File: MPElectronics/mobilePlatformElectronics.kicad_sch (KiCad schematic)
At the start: 40 parts, among them J1 UART, J2 CommandGenerator, M1 Motor_DC, M2 Motor_DC, Q1 LTR3208E, SW2 Reset, U1 PIC32MX170F256B, U2 L293NE/SN754410NE, U7 MCP6294, U8 LM339AN

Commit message: progress on schematic; complete pin assignment; most subsystems designed electrically
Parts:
- removed J2: CommandGenerator, symbol Connector:Conn_01x04_Socket
- removed M1, M2: Motor_DC, symbol Motor:Motor_DC_ALT
- added C10: 10uF, symbol ME218_BaseLib:Cap
- added C11, C12, C14, C15, C16, C7, C8, C9: 0.1uF, symbol ME218_BaseLib:Cap
- added J2: UART, symbol Connector:Conn_01x02_Socket
- added J3, J4: Magnetic Encoder, symbol Connector:Conn_01x04_Socket
- added M1 (x2), M2 (x2): Motor_DC, symbol Motor:Motor_DC_ALT
- added M3: SG90 9g Micro Servo, symbol ME218_BaseLib:Motor_Servo
- added M4, M5: Servo, symbol ME218_BaseLib:Motor_Servo
- added PRG2: MPLAB_Snap, symbol ME218_BaseLib:MPLAB_Snap
- added R12, R14: 1K, symbol ME218_BaseLib:Res2
- added R13, R15: 10K, symbol ME218_BaseLib:Res2
- added SW1, SW3: Reset, symbol ME218_BaseLib:SW-PB
- added SW4, SW5: SW_SPDT, symbol Switch:SW_SPDT
- added U10, U2: TLE5206-2S, TLE5206-2S:TO127P1000X440X1730-7, symbol TLE5206-2S:TLE5206-2S
- added U11, U12, U13: IR Distance, OptoDevice:Vishay_MINICAST-3Pin, symbol Sensor_Proximity:TSSP58038
- added U3: PIC32MX170F256B, symbol ME218_BaseLib:PIC32MX170F256B
- added U4, U5, U6, U9: IR Line Sensor, OptoDevice:Vishay_MINICAST-3Pin, symbol Sensor_Proximity:TSSP58038
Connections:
- net +3V3: now also C7.1, C8.2, J3.1 (Pin_1), J4.1 (Pin_1), PRG2.2 (Vdd), R13.2, R15.2, SW4.1 (A), SW5.1 (A), U11.3 (Vs), U12.3 (Vs), U13.3 (Vs), U3.13 (Vdd), U3.28 (AVdd), U4.3 (Vs), U5.3 (Vs), U6.3 (Vs), U9.3 (Vs)
- net +5V: now also U2.1 (EN1,2), U2.9 (EN3,4), C16.2, M3.2 (+), M4.2 (+), M5.2 (+); no longer C5.2
- net GND: now also C1.2, C2.1, C3.1, C4.2, C5.1, PRG1.3 (Vss), SW2.2, U1.19 (Vss), U1.27 (AVss), U1.8 (Vss), U2.10 (3A), U2.12 (GND), U2.13 (GND), U2.4 (GND), U2.5 (GND), U2.7 (2A), C10.1, C11.2, C12.1, C14.1, C15.1, C16.1, C7.2, C8.1, C9.2, J3.4 (Pin_4), J4.4 (Pin_4), M3.3 (-), M4.3 (-), M5.3 (-), PRG2.3 (Vss), SW1.2, SW3.2, SW4.3 (C), SW5.3 (C), U10.4 (GND), U11.2 (GND), U12.2 (GND), U13.2 (GND), U2.4 (GND), U3.19 (Vss), U3.27 (AVss), U3.8 (Vss), U4.2 (GND), U5.2 (GND), U6.2 (GND), U9.2 (GND)
- net GNDREF: no longer C1.2, C2.1, C3.1, C4.2, C5.1, PRG1.3 (Vss), SW2.2, U1.19 (Vss), U1.27 (AVss), U1.8 (Vss), U2.12 (GND), U2.13 (GND), U2.4 (GND), U2.5 (GND)
- net RX: now also J2.1 (Pin_1), U3.16 (5VT/RB7)
- net SPI1_SCK: now also U3.25 (RB14)
- net SPI1_SDI: now also U3.22 (RB11)
- net SPI1_SDO: now also U3.24 (RB13)
- net TX: now also J2.2 (Pin_2), U3.15 (PGEC3/5VT/RB6)
- net at D1.2 (A), D2.1 (K), D3.1 (KA)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: now also M1.1 (+)
- net at D10.2 (A), D11.1 (K), D12.1 (KA)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: now also M2.1 (+)
- net INT_LINE_FRONT_R: now reaches U1.9 (RA2)
- net INT_LINE_FRONT_R: now also U6.1 (OUT); no longer U2.1 (EN1,2)
- net at D13.2 (A), D14.1 (K), R23.1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: now also M2.2 (-)
- net at D4.2 (A), D5.1 (K), R3.1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: now also M1.2 (-)
- net DIN_LINE_PIVOT_L: now reaches U1.6 (RB2)
- net DIN_LINE_PIVOT_L: now also U4.1 (OUT); no longer U2.9 (EN3,4)
- net IC_DISTANCE: now reaches U1.14 (PGED3/5VT/RB5)
- net IC_DISTANCE: now also U11.1 (OUT)
- net M_DRIVE_L_PWM: now reaches U1.17 (5VT/RB8)
- net M_DRIVE_L_PWM: now also U2.3 (IN1)
- net M_DRIVE_R_PWM: now reaches U1.21 (PGEC2/5VT/RB10)
- net M_DRIVE_R_PWM: now also U10.3 (IN1)
- net M_DRIVE_R_DIR: now reaches U1.23 (RB12)
- net M_DRIVE_R_DIR: now also U10.5 (IN2)
- net DIN_LINE_PIVOT_R: now reaches U1.7 (RB3)
- net DIN_LINE_PIVOT_R: now also U9.1 (OUT)
- net IC renamed IC_BEACON
- net IC_BEACON: now also U1.12 (RA4); no longer U1.18 (PGED2/5VT/RB9)
- net LINE_OUT renamed INT_DRIVE_L
- net INT_DRIVE_L: now also J3.2 (Pin_2)
- net RA1, pin 3, OC2, Direction Pin renamed INT_DRIVE_R
- net INT_DRIVE_R: now also J4.2 (Pin_2); no longer U2.7 (2A)
- net RA3, pin 10, OC3 renamed INT_LINE_FRONT_L
- net INT_LINE_FRONT_L: now also U5.1 (OUT); no longer U2.10 (3A)
- net RA4, pin 12, OC4 or OC5, Direction Pin renamed M_INTAKE_PWM
- net M_INTAKE_PWM: now also U2.2 (1A), U3.6 (RB2); no longer U1.12 (RA4)
- net RB15, pin 26, OC1 renamed SPI1_~{CS}
- net SPI1_~{CS}: now also U3.26 (RB15); no longer U2.2 (1A)
- new net: PRG2.1 (~{MCLR}/Vpp), R14.1, U3.1 (~{MCLR})
- new net: PRG2.4 (PGData), U3.4 (PGED1/RB0)
- new net: PRG2.5 (PGClk), U3.5 (PGEC1/RB1)
- new net: C9.1, R12.2, R13.1, SW1.1
- new net: M1.1 (+), U2.1 (OUT1)
- new net: M1.2 (-), U2.7 (OUT2)
- new net: C11.1, R14.2, R15.1, SW3.1
- new net: C10.2, U3.20 (Vcap)
- new net: M2.1 (+), U10.1 (OUT1)
- new net: M2.2 (-), U10.7 (OUT2)
- new net +14V: C12.2, C14.2, C15.2, C5.2, U10.6 (VS), U2.6 (VS)
- new net DIN_CARGO_IN: U12.1 (OUT), U3.17 (5VT/RB8)
- new net DIN_CARGO_OUT: U13.1 (OUT), U3.18 (PGED2/5VT/RB9)
- new net DIN_GAMEMODE: SW4.2 (B), U3.11 (RB4)
- new net DIN_START: R12.1, U3.10 (RA3)
- new net DIN_STRATEGY: SW5.2 (B), U3.12 (RA4)
- new net M_ARM_ELBOW_PWM: M4.1 (PWM), U3.2 (RA0)
- new net M_ARM_HAND_PWM: M5.1 (PWM), U3.3 (RA1)
- new net M_BG_PWM: M3.1 (PWM), U3.21 (PGEC2/5VT/RB10)
- new net M_DRIVE_L_DIR: U1.18 (PGED2/5VT/RB9), U2.5 (IN2)
- new net M_FEEDER_PWM: U3.9 (RA2)
- new net bL: J3.3 (Pin_3)
- new net bR: J4.3 (Pin_3)
- no-connect marks 5 -> 7
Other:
- note removed: "Pololu QTR Reflectance Sensor"
- moved on the sheet: C1, C13, C2, C3, C4, C6, D1, D10, D11, D12, D13, D14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

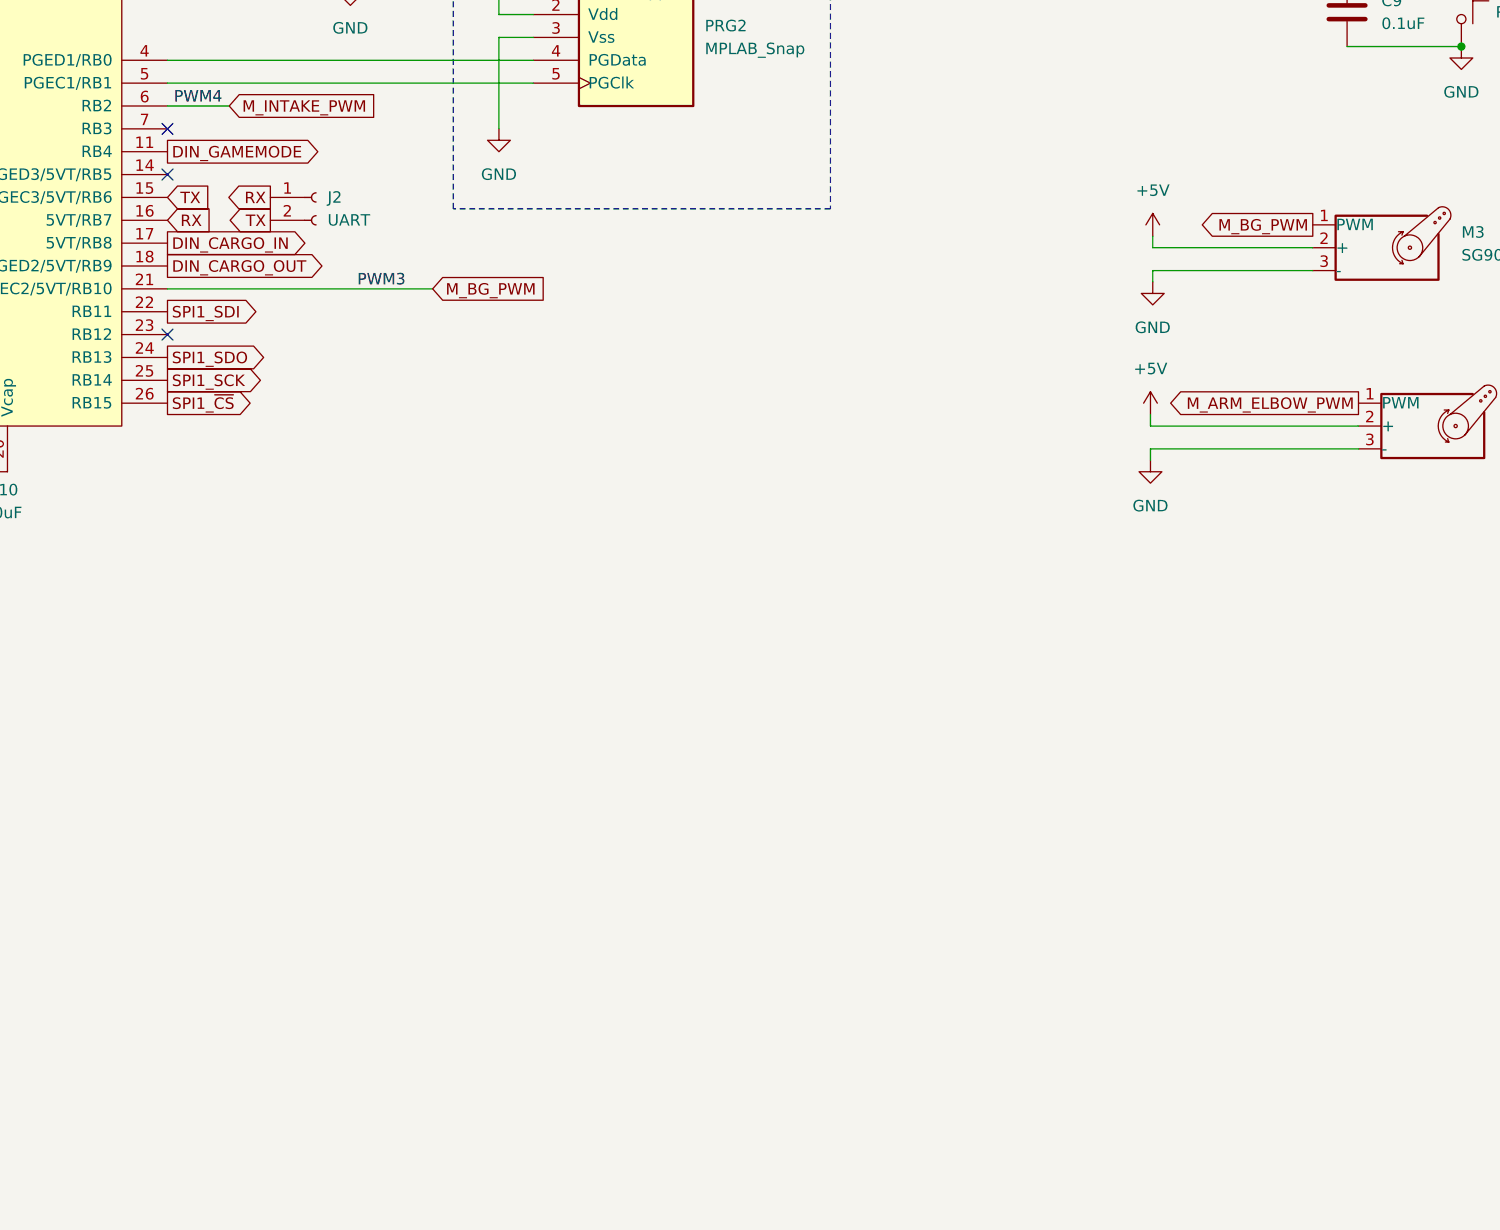
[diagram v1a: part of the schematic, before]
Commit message: update schematic
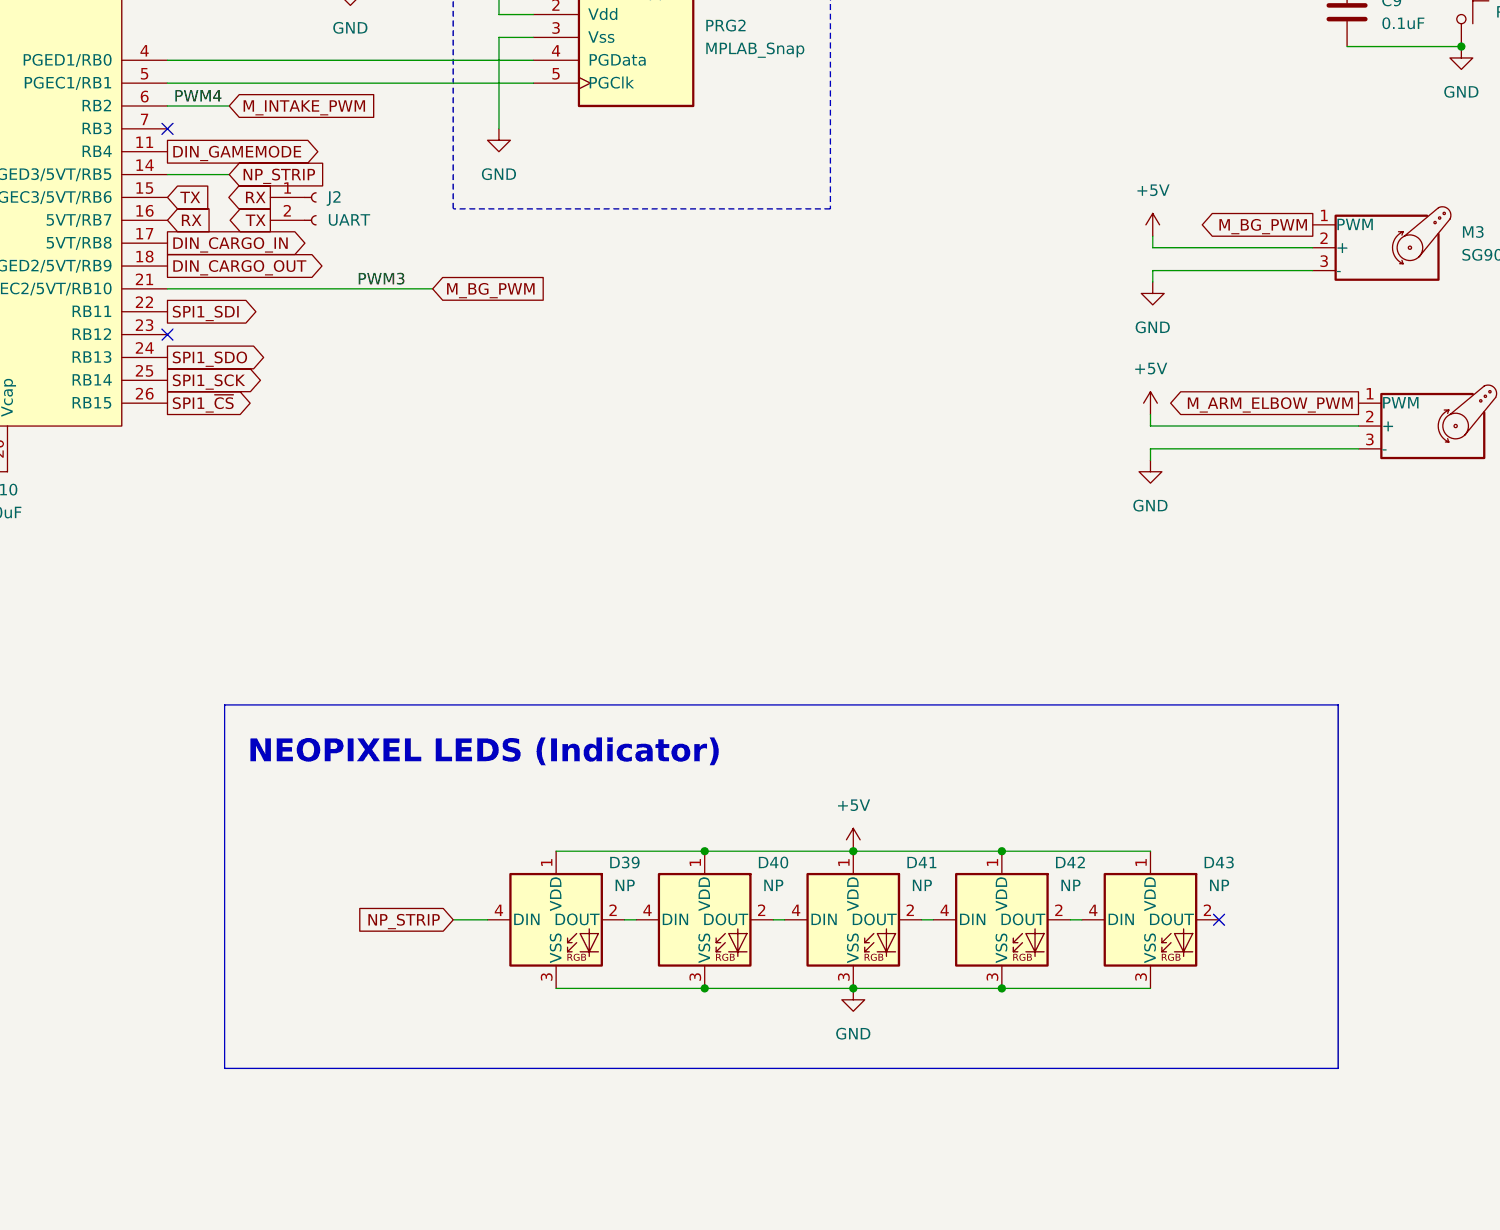
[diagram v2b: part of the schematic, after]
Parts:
- added D39, D40, D41, D42, D43: NP, LED_SMD:LED_WS2812B_PLCC4_5.0x5.0mm_P3.2mm, symbol LED:WS2812B
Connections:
- net +5V: now also D39.1 (VDD), D40.1 (VDD), D41.1 (VDD), D42.1 (VDD), D43.1 (VDD)
- net GND: now also D39.3 (VSS), D40.3 (VSS), D41.3 (VSS), D42.3 (VSS), D43.3 (VSS)
- net NP_STRIP: now reaches U3.14 (PGED3/5VT/RB5)
- net NP_STRIP: now also D39.4 (DIN)
- new net: D39.2 (DOUT), D40.4 (DIN)
- new net: D40.2 (DOUT), D41.4 (DIN)
- new net: D41.2 (DOUT), D42.4 (DIN)
- new net: D42.2 (DOUT), D43.4 (DIN)
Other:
- note added: "NEOPIXEL LEDS (Indicator)"

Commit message: include stepper driver and stepper in schematic
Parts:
- removed D12, D3: LED_Dual_Bidirectional, symbol Device:LED_Dual_Bidirectional
- removed R23, R3: 100, symbol ME218_BaseLib:Res2
- added A?: A4988_StepperDriver, Module:Pololu_Breakout-16_15.2x20.3mm, symbol Driver_Motor:Pololu_Breakout_A4988
- added M?: SY35ST28-0504A_Stepper_Motor_bipolar, symbol Motor:Stepper_Motor_bipolar
- C14, C5: value 0.1uF -> 470uF
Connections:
- net +14V: now also A?.8 (VMOT)
- net +3V3: now also A?.13 (~{RESET}), A?.14 (~{SLEEP}), A?.2 (VDD)
- net GND: now also A?.1 (GND), A?.16 (DIR), A?.7 (GND), A?.9 (~{ENABLE})
- net M_FEEDER_PWM: now also A?.15 (STEP)
- new net: A?.3 (1B), M?.2 (-)
- new net: A?.4 (1A), M?.1
- new net: A?.5 (2A), M?.3
- new net: A?.6 (2B), M?.4
- no-connect marks 7 -> 10
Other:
- moved on the sheet: D13, D14, D4, D5, M1, M2

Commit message: update schematic; 1 extra pin on drive; 2 extra pins on operator
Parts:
- removed U11: IR Distance, OptoDevice:Vishay_MINICAST-3Pin, symbol Sensor_Proximity:TSSP58038
- added C17: 100uF, symbol ME218_BaseLib:Cap
- added C18, C20: 0.1uF, symbol ME218_BaseLib:Cap
- added C19, C21: 4700uF, symbol ME218_BaseLib:Cap
- added R16, R18: 10K, symbol ME218_BaseLib:Res2
- added R17, R3: 1K, symbol ME218_BaseLib:Res2
- added SW6, SW7: SW_SPDT_LIMIT, symbol Switch:SW_SPDT_XKB_DMx-xxxx-1
- M6: renamed from M4; value Servo -> RDS51150
- M7: renamed from M5; value Servo -> RDS51150
- gave numbers to parts that had none: 2
- renumbered M1 to M3, M2 to M4, M3 to M5, U2 to U14
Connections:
- net +14V: now also C17.2
- net +3V3: now also R16.2, R18.2
- net +5V: no longer M6.2 (+), M7.2 (+)
- net GND: now also C17.1, C18.2, C19.2, C20.2, C21.2, SW6.2 (B), SW7.2 (B)
- net IC_DISTANCE renamed DIN_LIMIT
- net DIN_LIMIT: now also R3.1
- net SPI1_~{SS}: no longer names the net of U1.11 (RB4)
- new net: C20.1, R17.2, R18.1, SW7.1 (A)
- new net: C18.1, R16.1, R3.2, SW6.1 (A)
- new net +12V: C19.1, C21.1, M6.2 (+), M7.2 (+)
- new net DIN_ARM_LIMIT: R17.1
- no-connect marks 10 -> 13
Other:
- note added: "Follow PIC32"
- note added: "Lead PIC32"
- note added: "State Indicator Neopixel"
- note removed: "NEOPIXEL LEDS (Indicator)"
- moved on the sheet: A1, C12, C13, C14, C15, C16, C5, C6, D1, D10, D11, D13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

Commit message: reorganize schematic, label for ease of construction, include improved beacon sensing AFE
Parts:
- added C?: 0.1uF, symbol ME218_BaseLib:Cap
- added R?: 1K, symbol ME218_BaseLib:Res2
- added R?: 470K, symbol ME218_BaseLib:Res2
- added R?: 2K, symbol ME218_BaseLib:Res2
- added unit 4 of U7
- R7: value 100K -> 2K
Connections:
- net +12V is gone; now on net +5V: C19.1, C21.1, M6.2 (+), M7.2 (+)
- net GNDREF is gone; now on net GND: D11.2 (A), D14.2 (A), D2.2 (A), D5.2 (A)
- net +3V3: now also U7.4 (V+)
- net +5V: now also U7.4 (V+); no longer Q1.1 (C), U7.4 (V+)
- net DIN_ARM_LIMIT: now also U3.7 (RB3)
- net DIN_LIMIT: now also U1.12 (RA4); no longer U1.14 (PGED3/5VT/RB5)
- net GND: now also Q1.2 (E), U7.11 (V-)
- net IC_BEACON: now also U1.14 (PGED3/5VT/RB5); no longer U1.12 (RA4)
- net Vref: now reaches R6.1, U7.6 (-), U7.7
- net Vref: now also R?.1, R?.2
- net at R7.1, U7.2 (-): now also Q1.1 (C); no longer Q1.2 (E)
- net at R7.2, U7.1: now also C?.2; no longer U8.4 (-)
- new net: R?.1, R?.2, U7.13 (-)
- new net: R?.2, U7.14, U8.4 (-)
- new net: C?.1, R?.1, U7.12 (+)
- no-connect marks 13 -> 12
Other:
- note added: "2-joint Arm"
- note added: "Cargo Handling"
- note added: "Cargo Sensing"
- note added: "Comparator with Hysteresis"
- note added: "DC Motors and Drivers"
- note added: "Drive Train"
- note added: "Drive and Navigation"
- note added: "Feeder"
- note added: "Field Side Indicator"
- note added: "First Stage (Transimpedance) Amplifier"
- note added: "High Pass Filter"
- note added: "IR Beacon Sensor (Phototransistor) and Analog Front End"
- note added: "IR Tape Sensors"
- note added: "Inputs"
- note added: "Intake"
- note added: "Limit Switch"
- note added: "Magnetic Encoder"
- note added: "Operation and Manipulation"
- note added: "Outputs"
- note added: "Reference voltage buffer"
- note added: "Second Stage (Noninverting) Amplifier"
- note added: "Sensing for Navigation"
- note added: "User Interface"
- title: Test sheet -> Mobile Platform
- moved on the sheet: A1, C1, C10, C11, C12, C13, C14, C15, C16, C17, C18, C19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

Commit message: update signal conditioning circuit
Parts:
- gave numbers to parts that had none: 4
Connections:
- net +3V3: now also U7.4 (V+), U7.4 (V+), U7.4 (V+), U8.3 (V+)
- net +5V: no longer U7.4 (V+), U7.4 (V+), U7.4 (V+), U8.3 (V+)
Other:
- note added: "High Pass Filter fc = 530.5 Hz"
- note removed: "High Pass Filter"
- moved on the sheet: C10, C11, C13, C18, C22, C6, C7, C8, J2, PRG2, Q1, R10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
